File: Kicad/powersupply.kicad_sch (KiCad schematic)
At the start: 19 parts, among them J1701 Jack 2/6.3mm, Q1701 BC546, Q1702 BC556, U1701 DC-DC Module, U1702 MAX1615, U1703 TLV1117 3.3V 1A

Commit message: Update schematic files to Kicad 6.
Had to fix some symbols which didn't have perfect matches in K6.
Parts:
- C12001: renamed from C1701; symbol Neotron-Common-Hardware-rescue:CP-Device -> Device:C_Polarized
- C12002: renamed from C1702; symbol Neotron-Common-Hardware-rescue:CP-Device -> Device:C_Polarized
- renumbered C1703 to C12003, C1704 to C12004, C1705 to C12005, C1706 to C12006, C1707 to C12007, C1708 to C12008, F1701 to F12001, J1701 to J12001, L1701 to L12001, Q1701 to Q12001, Q1702 to Q12002, R1701 to R12001, R1702 to R12002, R1703 to R12003, U1701 to U12001, U1702 to U12002, U1703 to U12003
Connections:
- net +3V3 renamed +3.3V

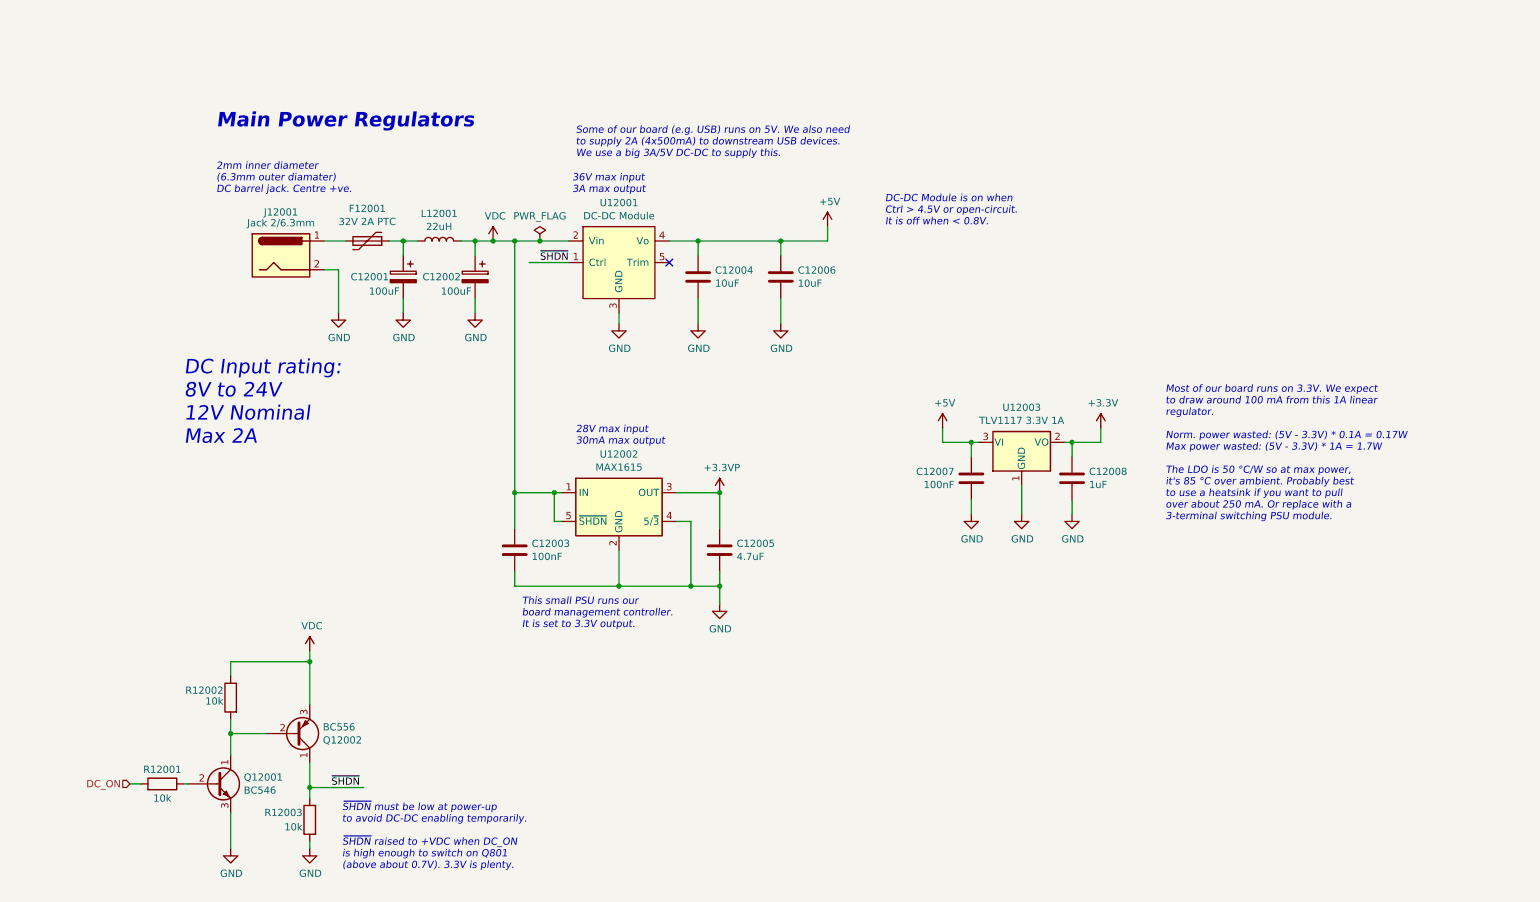
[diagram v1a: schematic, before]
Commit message: Imported sheets from Neotron Pico.
Standardised on +3V3 not +3.3V
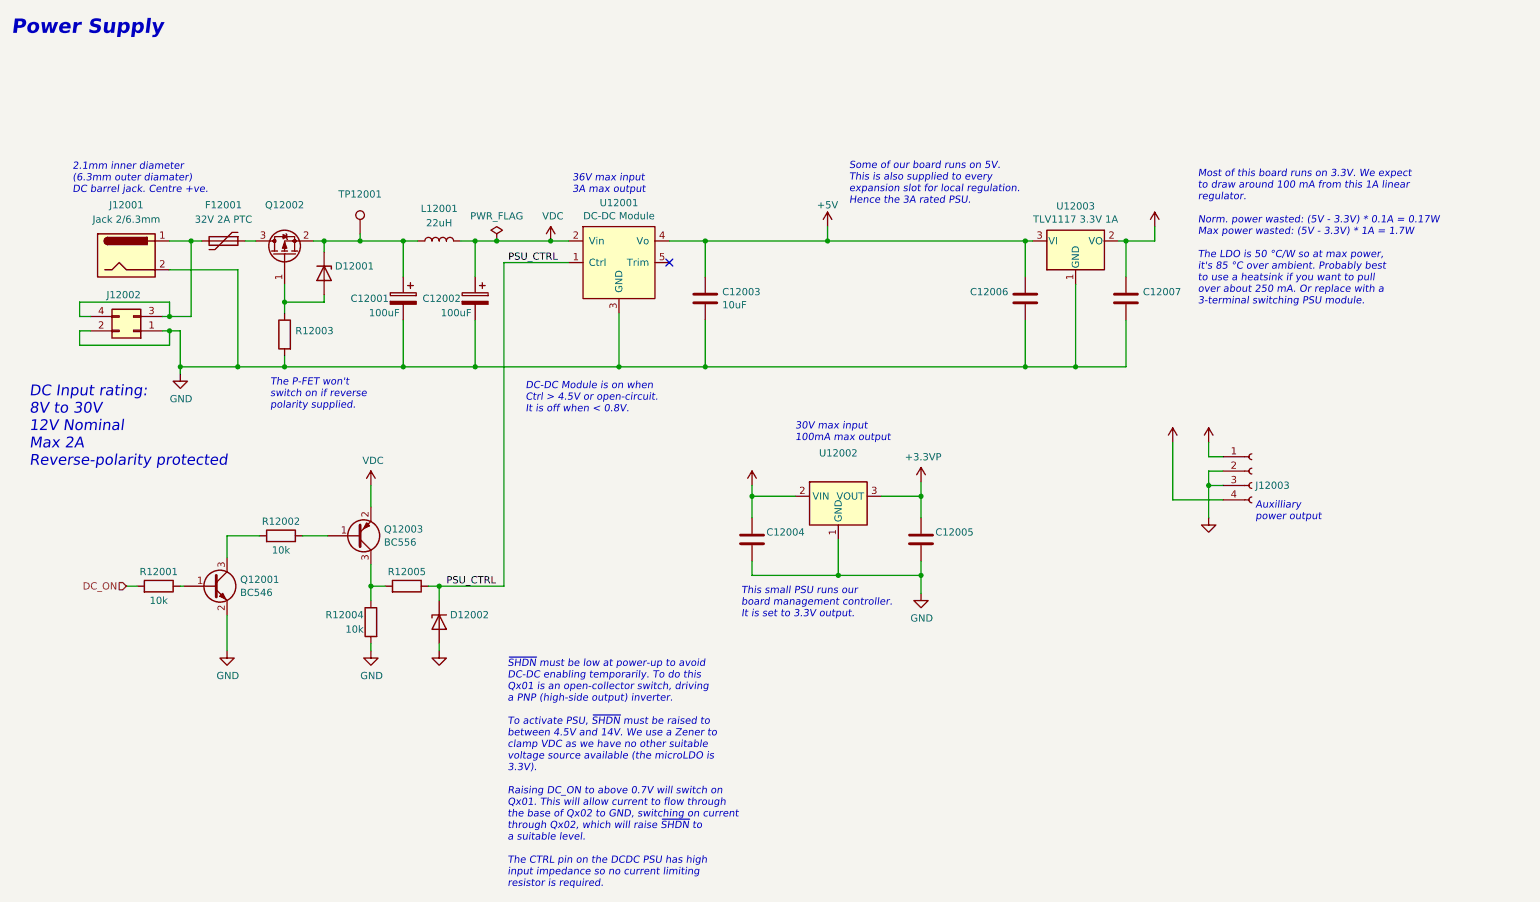
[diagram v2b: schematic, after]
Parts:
- removed C12003: 100nF, Capacitor_SMD:C_0805_2012Metric_Pad1.18x1.45mm_HandSolder, symbol Device:C
- removed C12008: 1uF, Capacitor_SMD:C_0805_2012Metric_Pad1.18x1.45mm_HandSolder, symbol Device:C
- removed U12002: MAX1615, Package_TO_SOT_SMD:SOT-23-5, symbol Regulator_Linear:MAX1615xUK
- added C12004: (no value), symbol Device:C
- added D12001, D12002: (no value), symbol Diode:ZMMxx
- added J12002: (no value), symbol Connector_Generic:Conn_02x02_Odd_Even
- added J12003: (no value), symbol Connector:Conn_01x04_Female
- added Q12002: (no value), symbol Transistor_FET:AO3401A
- added R12003, R12005: (no value), symbol Device:R
- added TP12001: (no value), symbol Connector:TestPoint
- added U12002: (no value), symbol Regulator_Linear:HT75xx-1-SOT89
- C12001, C12002: Digikey (none) -> P5182-ND; MPN CPL-CAP-ALU-RAD-100UF-50V -> ECA-1HM101; Manufacturer CPL -> Panasonic; Mouser (none) -> 667-ECA-1HM101
- C12003: renamed from C12004; JLCPCB Collection (none) -> Extended; LCSC Part# C15850 -> C602037; MPN CPL-CAP-X5R-0805-10UF-16V -> CL21A226MAYNNNE; Manufacturer CPL -> Samsung; Voltage 16V -> 25V
- C12005: value 4.7uF -> (none); footprint Capacitor_SMD:C_0805_2012Metric_Pad1.18x1.45mm_HandSolder -> (none); JLCPCB Collection (none) -> Basic; LCSC Part# C1779 -> C15850; MPN CPL-CAP-X5R-0805-4.7UF-25V -> CL21A106KAYNNNE; Manufacturer CPL -> Samsung; Voltage 10V -> 25V
- C12006: value 10uF -> (none); footprint Capacitor_SMD:C_0805_2012Metric_Pad1.18x1.45mm_HandSolder -> (none); JLCPCB Collection (none) -> Extended; LCSC Part# C15850 -> C602037; MPN CPL-CAP-X5R-0805-10UF-16V -> CL21A226MAYNNNE; Manufacturer CPL -> Samsung; Voltage 16V -> 25V
- C12007: value 100nF -> (none); footprint Capacitor_SMD:C_0805_2012Metric_Pad1.18x1.45mm_HandSolder -> (none); JLCPCB Collection (none) -> Extended; LCSC Part# C49678 -> C602037; MPN CPL-CAP-X7R-0805-100NF-50V -> CL21A226MAYNNNE; Manufacturer CPL -> Samsung; Voltage 16V -> 25V
- L12001: Tolerance 2A -> (none)
- Q12001: symbol Transistor_BJT:BC546 -> Transistor_BJT:BC817; Digikey BC546CTACT-ND -> (none); JLCPCB Collection (none) -> Basic; LCSC Part# (none) -> C2150; MPN BC546CTA -> SS8050; Manufacturer ON Semiconductor -> JSCJ; Mouser 512-BC546CTA -> (none); Voltage (none) -> 25V
- Q12003: renamed from Q12002; symbol Transistor_BJT:BC556 -> Transistor_BJT:BC807; Digikey BC556BTFCT-ND -> (none); JLCPCB Collection (none) -> Basic; LCSC Part# (none) -> C8542; MPN BC556BTF -> SS8550 Y2; Manufacturer ON Semiconductor -> JSCJ; Mouser 512-BC556BTF -> (none); Voltage (none) -> 25V
- R12001, R12002: JLCPCB Collection (none) -> Basic; MPN CPL-RES-0805-10K-0.125W -> 0805W8F1002T5E; Manufacturer CPL -> Uniroyal
- R12004: renamed from R12003; JLCPCB Collection (none) -> Basic; MPN CPL-RES-0805-10K-0.125W -> 0805W8F1002T5E; Manufacturer CPL -> Uniroyal
- U12003: JLCPCB Collection (none) -> Basic; MPN CPL-REG-LIN-3.3V-1A -> AMS1117-3.3; Manufacturer CPL -> AMS
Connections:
- net +3.3VP: now also C12005.2, U12002.3 (VOUT); no longer C12005.1
- net +5V: now also J12003.4 (Pin_4); no longer C12007.1
- net GND: now also C12005.1, Q12001.2 (E), C12004.1, D12002.2 (A), J12002.1 (Pin_1), J12002.2 (Pin_2), J12003.2 (Pin_2), J12003.3 (Pin_3), R12003.2, U12002.1 (GND); no longer C12005.2, Q12001.3 (E)
- net VDC: now also Q12003.2 (E), C12004.2, U12002.2 (VIN); no longer Q12003.3 (E), R12002.1
- net at C12001.1, L12001.1: now also D12001.1 (K), Q12002.2 (S), TP12001.1; no longer F12001.1
- net at F12001.2, J12001.1: now also J12002.3 (Pin_3), J12002.4 (Pin_4)
- net at R12001.1: now also Q12001.1 (B); no longer Q12001.2 (B)
- net +3.3V renamed +3V3
- net +3V3: now also C12007.1, J12003.1 (Pin_1)
- removed net ~{SHDN}: Q12003.1 (C), R12004.1, U12001.1 (Ctrl)
- new net: F12001.1, Q12002.3 (D)
- new net: Q12003.3 (C), R12004.1, R12005.2
- new net: Q12001.3 (C), R12002.2
- new net: Q12003.1 (B), R12002.1
- new net: D12001.2 (A), Q12002.1 (G), R12003.1
- new net PSU_CTRL: D12002.1 (K), R12005.1, U12001.1 (Ctrl)
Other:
- note added: "2.1mm inner diameter (6.3mm outer diamater) DC barrel jack. Centre +ve."
- note added: "30V max input 100mA max output"
- note added: "Auxilliary power output"
- note added: "DC Input rating: 8V to 30V 12V Nominal Max 2A Reverse-polarity protected"
- note added: "Most of this board runs on 3.3V. We expect to draw around 100 mA from this 1A linear regulator. Norm. power wasted: (5V - 3.3V) * 0.1A = 0.17W Max power wasted: (5V - 3.3V) * 1A = 1.7W The LDO is 50 °C/W so at max power, it's 85 °C over ambient. Probably best to use a heatsink if you want to pull over about 250 mA. Or replace with a 3-terminal switching PSU module."
- note added: "Power Supply"
- note added: "Some of our board runs on 5V. This is also supplied to every expansion slot for local regulation. Hence the 3A rated PSU."
- note added: "The P-FET won't switch on if reverse polarity supplied."
- note added: "~{SHDN} must be low at power-up to avoid DC-DC enabling temporarily. To do this Qx01 is an open-collector switch, driving a PNP (high-side output) inverter. To activate PSU, ~{SHDN} must be raised to between 4.5V and 14V. We use a Zener to clamp VDC as we have no other suitable voltage source available (the microLDO is 3.3V). Raising DC_ON to above 0.7V will switch on Qx01. This will allow curren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"
- note removed: "28V max input 30mA max output"
- note removed: "2mm inner diameter (6.3mm outer diamater) DC barrel jack. Centre +ve."
- note removed: "DC Input rating: 8V to 24V 12V Nominal Max 2A"
- note removed: "Main Power Regulators"
- note removed: "Most of our board runs on 3.3V. We expect to draw around 100 mA from this 1A linear regulator. Norm. power wasted: (5V - 3.3V) * 0.1A = 0.17W Max power wasted: (5V - 3.3V) * 1A = 1.7W The LDO is 50 °C/W so at max power, it's 85 °C over ambient. Probably best to use a heatsink if you want to pull over about 250 mA. Or replace with a 3-terminal switching PSU module."
- note removed: "Some of our board (e.g. USB) runs on 5V. We also need to supply 2A (4x500mA) to downstream USB devices. We use a big 3A/5V DC-DC to supply this."
- note removed: "~{SHDN} must be low at power-up to avoid DC-DC enabling temporarily. ~{SHDN} raised to +VDC when DC_ON is high enough to switch on Q801 (above about 0.7V). 3.3V is plenty."
- company: https://neotron-compute.github.io/ -> https://neotron-compute.github.io
- moved on the sheet: C12001, C12002, C12003, F12001, J12001, Q12003, R12001, R12002, R12004, U12003

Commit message: Set missing footprints and update PCB
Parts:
- C12001, C12002: value 100uF -> 100u
- C12003: value 10uF -> 10u; JLCPCB Collection Extended -> (none); LCSC Part# C602037 -> (none); MPN CL21A226MAYNNNE -> (none); Manufacturer Samsung -> (none)
- C12004, C12005: value (none) -> 10u; footprint (none) -> Capacitor_SMD:C_0805_2012Metric_Pad1.18x1.45mm_HandSolder; JLCPCB Collection Basic -> (none); LCSC Part# C15850 -> (none); MPN CL21A106KAYNNNE -> (none); Manufacturer Samsung -> (none)
- C12006, C12007: value (none) -> 22u; footprint (none) -> Capacitor_SMD:C_0805_2012Metric_Pad1.18x1.45mm_HandSolder
- D12001, D12002: value (none) -> ZMM5V6; footprint (none) -> Diode_SMD:D_MiniMELF
- J12002: value (none) -> Conn_02x02S; footprint (none) -> Connector_PinSocket_2.54mm:PinSocket_2x02_P2.54mm_Vertical
- J12003: value (none) -> Conn_01x04S; footprint (none) -> Connector_PinSocket_2.54mm:PinSocket_1x04_P2.54mm_Vertical
- Q12002: value (none) -> AO3401A; footprint (none) -> Package_TO_SOT_SMD:SOT-23
- R12003: value (none) -> 10k; footprint (none) -> Resistor_SMD:R_0805_2012Metric_Pad1.20x1.40mm_HandSolder
- R12005: value (none) -> 1k; footprint (none) -> Resistor_SMD:R_0805_2012Metric_Pad1.20x1.40mm_HandSolder
- TP12001: value (none) -> PTH; footprint (none) -> TestPoint:TestPoint_Plated_Hole_D2.0mm
- U12002: value (none) -> HT75xx-1-SOT89; footprint (none) -> Package_TO_SOT_SMD:SOT-89-3

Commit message: Re-imported from Neotron Pico v1.1.
This time I deleted the sheets from the top level and then re-added pointing at the new files. I also reset the PCB dimensions to match the Neotron Pico.

This seems to have done a better job importing footprints.
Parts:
- C403: renamed from C12003; value 10u -> 22u; JLCPCB Collection (none) -> Extended; LCSC Part# (none) -> C602037; MPN (none) -> CL21A226MAYNNNE; Manufacturer (none) -> Samsung
- C404: renamed from C12004; JLCPCB Collection (none) -> Basic; LCSC Part# (none) -> C15850; MPN (none) -> CL21A106KAYNNNE; Manufacturer (none) -> Samsung
- C405: renamed from C12005; JLCPCB Collection (none) -> Basic; LCSC Part# (none) -> C15850; MPN (none) -> CL21A106KAYNNNE; Manufacturer (none) -> Samsung
- F401: renamed from F12001; footprint Fuse:Fuse_BelFuse_0ZRE0016FF_L9.9mm_W3.8mm -> Neotron-Common-Hardware:Bel Fuse 0ZRS0200FF
- J401: renamed from J12001; value Jack 2/6.3mm -> Jack 2.1mm 6.3mm
- Q401: renamed from Q12001; value BC546 -> SS8050; footprint Package_TO_SOT_THT:TO-92_Inline -> Package_TO_SOT_SMD:SOT-23
- Q403: renamed from Q12003; value BC556 -> SS8550; footprint Package_TO_SOT_THT:TO-92_Inline -> Package_TO_SOT_SMD:SOT-23
- TP401: renamed from TP12001; footprint TestPoint:TestPoint_Plated_Hole_D2.0mm -> TestPoint:TestPoint_THTPad_D1.5mm_Drill0.7mm
- U403: renamed from U12003; value TLV1117 3.3V 1A -> AMS1117-3.3
- renumbered C12001 to C401, C12002 to C402, C12006 to C406, C12007 to C407, D12001 to D401, D12002 to D402, J12002 to J402, J12003 to J403, L12001 to L401, Q12002 to Q402, R12001 to R401, R12002 to R402, R12003 to R403, R12004 to R404, R12005 to R405, U12001 to U401, U12002 to U402
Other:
- company: https://neotron-compute.github.io -> https://neotron-compute.github.io/
